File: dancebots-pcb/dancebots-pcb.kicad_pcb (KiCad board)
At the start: 2 copper layers, 50 x 50 mm, 33 parts, among them J1 BATTERY, J2 MOT2-L, J3 MOT1-R, J4 MP3 Player, U1 L4941, U2 L293, U3 ATTINY861A-P, U4 LM386, U5 LM358

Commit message: fixed silkscreen text to 2018 and 7.1
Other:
- board text added: "MP3 DanceBot V7.1 MINT&Pepper 2018"
- board text removed: "MP3 DanceBot V7 MINT&Pepper 2017"
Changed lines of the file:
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@@
   (page A4)
   (layers
-    (0 F.Cu signal)
-    (31 B.Cu signal)
+    (0 F.Cu signal hide)
+    (31 B.Cu signal hide)
     (32 B.Adhes user hide)
     (33 F.Adhes user hide)
     (34 B.Paste user hide)
     (35 F.Paste user hide)
-    (36 B.SilkS user)
+    (36 B.SilkS user hide)
     (37 F.SilkS user)
-    (38 B.Mask user)
-    (39 F.Mask user)
+    (38 B.Mask user hide)
+    (39 F.Mask user hide)
     (40 Dwgs.User user)
     (41 Cmts.User user)
@@
       (drillshape 0)
       (scaleselection 1)
-      (outputdirectory gerberv7.03/))
+      (outputdirectory gerberv7.1/))
   )
   (net 0 "")
@@
     (effects (font (size 1.2 1.2) (thickness 0.17)))
   )
-  (gr_text "MP3 DanceBot V7\nMINT&Pepper 2017" (at 147.75 101.95 90) (layer B.SilkS)
+  (gr_text "MP3 DanceBot V7.1\nMINT&Pepper 2018" (at 147.75 101.95 90) (layer B.SilkS)
     (effects (font (size 1.1 1.1) (thickness 0.17)) (justify left mirror))
   )

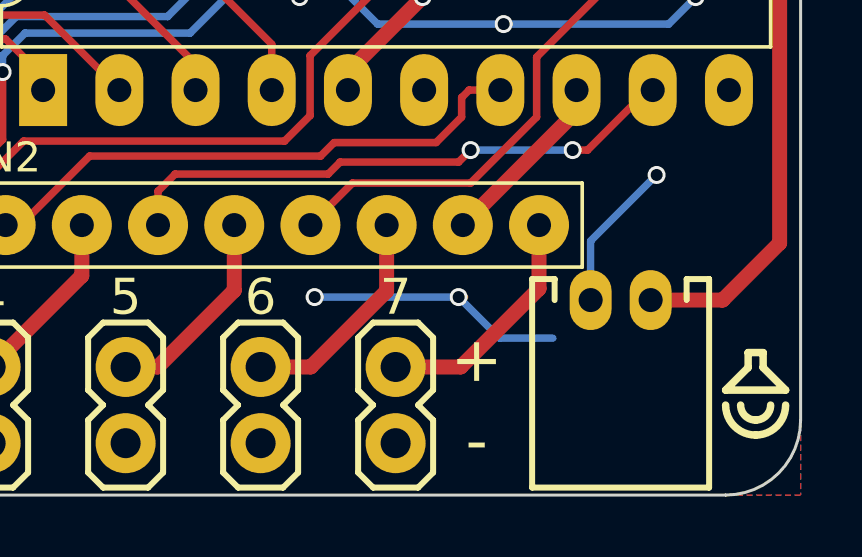
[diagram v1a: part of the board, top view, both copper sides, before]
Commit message: fixed broken ground plane connector near SPKR
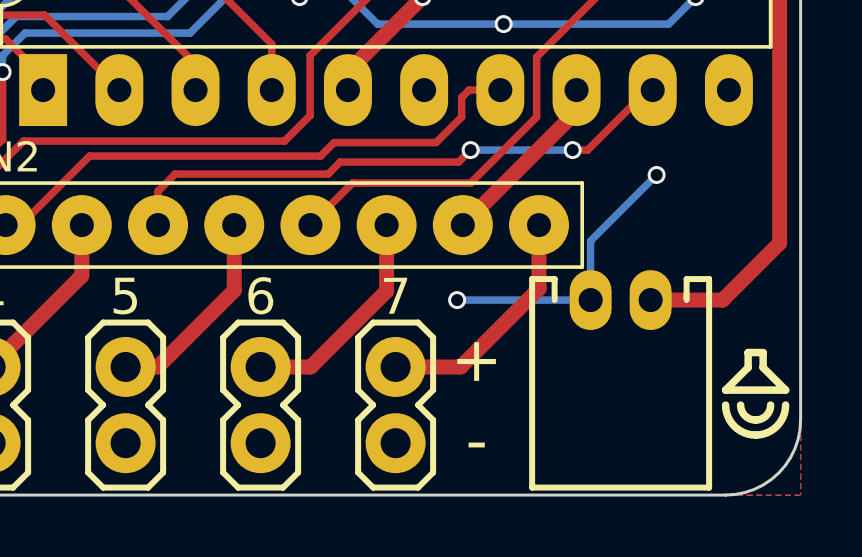
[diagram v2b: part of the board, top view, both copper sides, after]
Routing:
- net (no net): track 8.85 -> 0.00 mm, vias 2 -> 0
- net GND: track 173.4 -> 177.9 mm, vias 28 -> 29
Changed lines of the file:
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@@
     (thickness 1.6)
     (drawings 61)
-    (tracks 511)
+    (tracks 506)
     (zones 0)
     (modules 33)
@@
   (page A4)
   (layers
-    (0 F.Cu signal hide)
-    (31 B.Cu signal hide)
+    (0 F.Cu signal)
+    (31 B.Cu signal)
     (32 B.Adhes user hide)
     (33 F.Adhes user hide)
@@
   (gr_arc (start 102.5 102.5) (end 100 102.5) (angle 90) (layer Edge.Cuts) (width 0.1))
   (gr_line (start 102.5 100) (end 147.5 100) (angle 90) (layer Edge.Cuts) (width 0.1))
-  (segment (start 139.97 144.77) (end 138.6 143.4) (width 0.25) (layer B.Cu) (net 0))
-  (segment (start 141.74 144.77) (end 139.97 144.77) (width 0.25) (layer B.Cu) (net 0))
-  (segment (start 138.6 143.4) (end 133.8 143.4) (width 0.25) (layer B.Cu) (net 0))
-  (via (at 133.8 143.4) (size 0.6) (drill 0.4) (layers F.Cu B.Cu) (net 0))
-  (segment (start 138.6 143.4) (end 138.8 143.4) (width 0.25) (layer F.Cu) (net 0))
-  (via (at 138.6 143.4) (size 0.6) (drill 0.4) (layers F.Cu B.Cu) (net 0))
-  (segment (start 138.7 143.5) (end 138.6 143.4) (width 0.25) (layer B.Cu) (net 0))
   (segment (start 103.33 102.2) (end 103.33 105.87) (width 0.5) (layer F.Cu) (net 1))
   (segment (start 103.33 105.87) (end 103.3 105.9) (width 0.5) (layer F.Cu) (net 1))
@@
   (segment (start 103.4 119.7) (end 100.9 122.2) (width 0.5) (layer F.Cu) (net 1))
   (segment (start 103.4 117.44) (end 103.4 119.7) (width 0.5) (layer F.Cu) (net 1))
+  (segment (start 143 143.5) (end 138.55 143.5) (width 0.25) (layer B.Cu) (net 2) (status 400000))
+  (via (at 138.55 143.5) (size 0.6) (drill 0.4) (layers F.Cu B.Cu) (net 2))
   (segment (start 109.75 103.5) (end 108.3 103.5) (width 0.25) (layer F.Cu) (net 2))
   (segment (start 106.9 103.3) (end 107.65 104.05) (width 0.5) (layer B.Cu) (net 2))

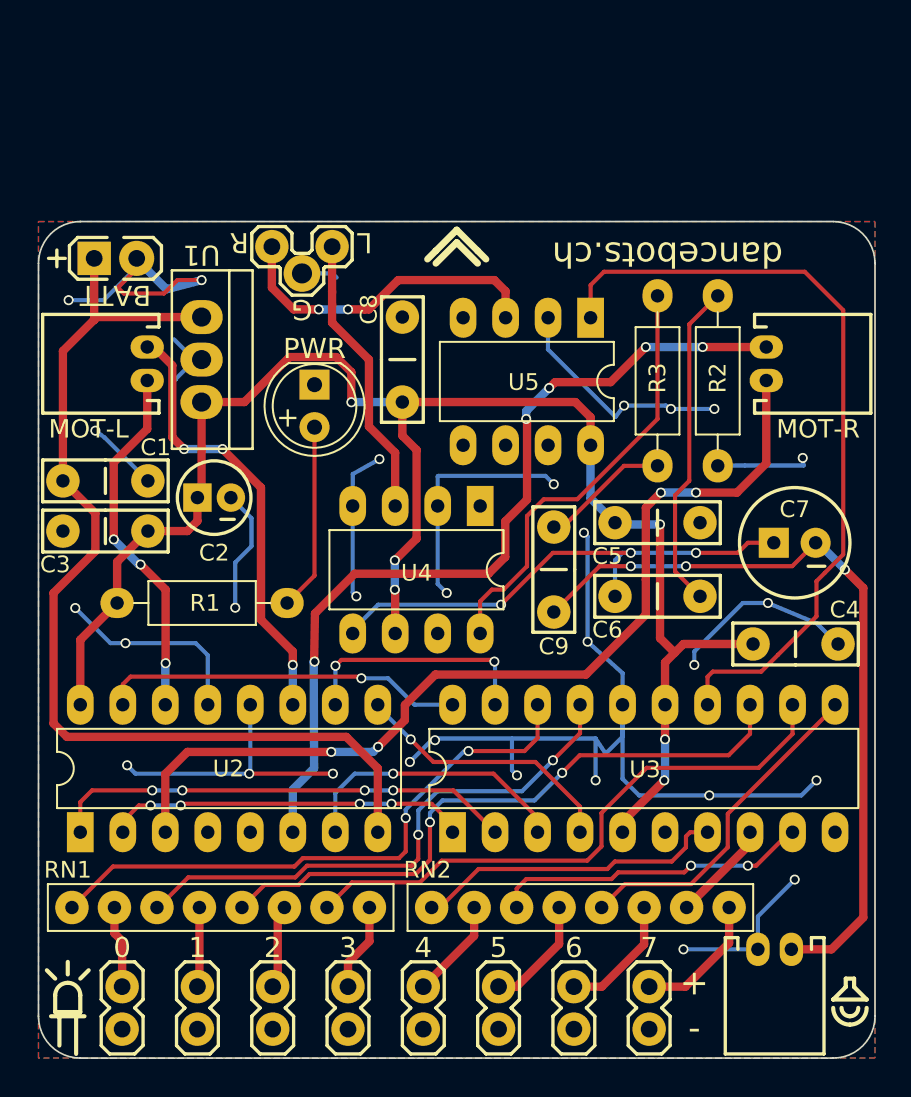
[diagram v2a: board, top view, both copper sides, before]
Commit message: v7.2: fixed symbol and library references, added part numbers, and cleaned up gnd vias on PCB
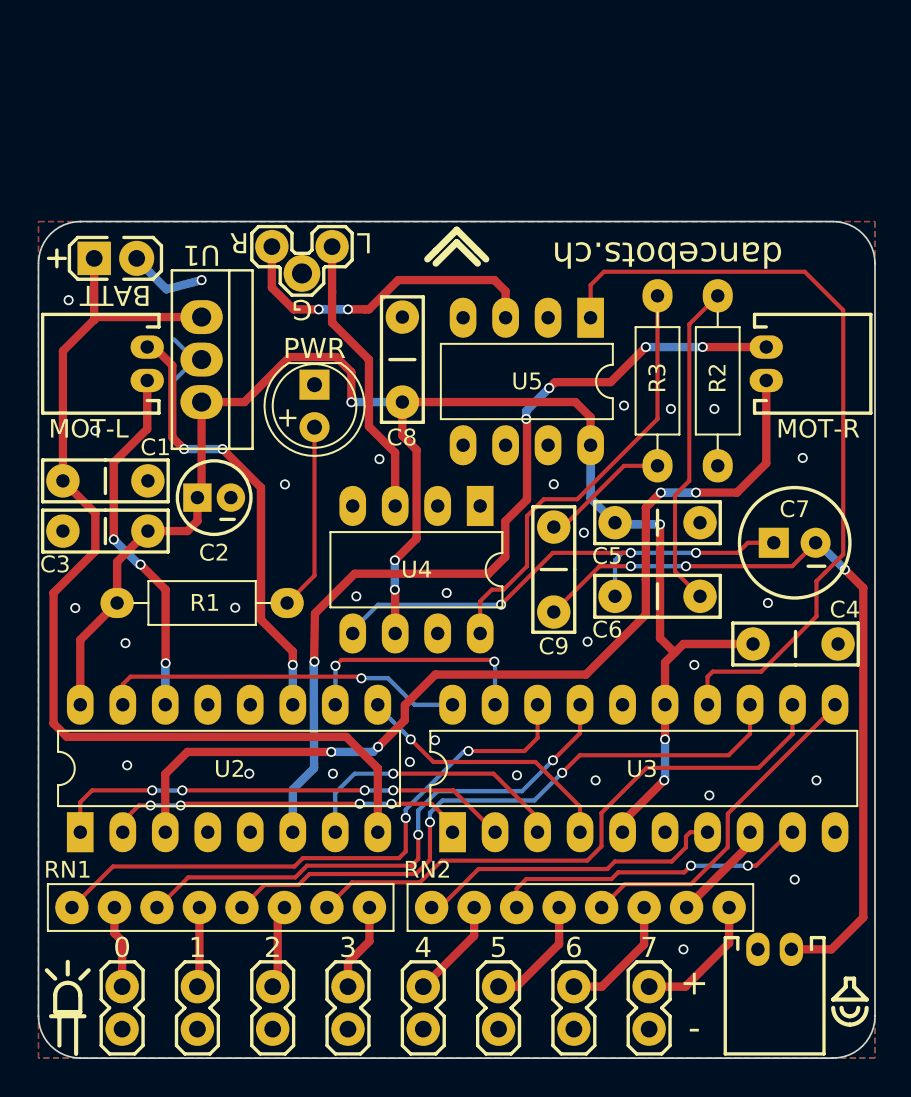
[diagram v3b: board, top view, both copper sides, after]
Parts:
- D0: footprint LEDs:LED_D5.0mm -> LED_THT:LED_D5.0mm
- U2: footprint Housings_DIP:DIP-16_W7.62mm_LongPads -> Package_DIP:DIP-16_W7.62mm_LongPads
- U3: value ATTINY861A-P -> ATTINY261A-P; footprint Housings_DIP:DIP-20_W7.62mm_LongPads -> Package_DIP:DIP-20_W7.62mm_LongPads
- U4, U5: footprint Housings_DIP:DIP-8_W7.62mm_LongPads -> Package_DIP:DIP-8_W7.62mm_LongPads
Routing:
- net GND: track 177.9 -> 10.9 mm, vias 29 -> 30
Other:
- board text added: "MP3 DanceBot V7.2 mint & pepper 2019"
- board text removed: "MP3 DanceBot V7.1 MINT&Pepper 2018"

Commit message: updated readme and added CERN license (also to PCB silkscreen)
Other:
- board text added: "Licensed under CERN OHL v.1.2"
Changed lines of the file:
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@@
   (general
     (thickness 1.6)
-    (drawings 61)
+    (drawings 62)
     (tracks 433)
     (zones 0)
@@
       (net 6 "Net-(C7-Pad2)"))
   )
+  (gr_text "Licensed under CERN OHL v.1.2" (at 132.512 100.978 180) (layer B.SilkS)
+    (effects (font (size 1.1 1.1) (thickness 0.17)) (justify mirror))
+  )
   (gr_line (start 123.75 101.75) (end 123.25 102.25) (angle 90) (layer F.SilkS) (width 0.4))
   (gr_line (start 126.25 101.75) (end 126.75 102.25) (angle 90) (layer F.SilkS) (width 0.4))
@@
     (effects (font (size 1.5 1.5) (thickness 0.2)))
   )
-  (gr_text "Designed in Switzerland" (at 135.1 102.05 180) (layer B.SilkS)
+  (gr_text "Designed in Switzerland" (at 129.21 102.756 180) (layer B.SilkS)
     (effects (font (size 1.1 1.1) (thickness 0.17)) (justify mirror))
   )
@@
   (gr_arc (start 102.5 102.5) (end 100 102.5) (angle 90) (layer Edge.Cuts) (width 0.1))
   (gr_line (start 102.5 100) (end 147.5 100) (angle 90) (layer Edge.Cuts) (width 0.1))
-  (via (at 114.732 115.71) (size 0.6) (drill 0.4) (layers F.Cu B.Cu) (net 2))
   (segment (start 103.33 102.2) (end 103.33 105.87) (width 0.5) (layer F.Cu) (net 1))
   (segment (start 103.33 105.87) (end 103.3 105.9) (width 0.5) (layer F.Cu) (net 1))
@@
   (segment (start 103.4 119.7) (end 100.9 122.2) (width 0.5) (layer F.Cu) (net 1))
   (segment (start 103.4 117.44) (end 103.4 119.7) (width 0.5) (layer F.Cu) (net 1))
+  (via (at 114.732 115.71) (size 0.6) (drill 0.4) (layers F.Cu B.Cu) (net 2))
   (via (at 138.55 143.5) (size 0.6) (drill 0.4) (layers F.Cu B.Cu) (net 2))
   (segment (start 106.9 103.3) (end 107.65 104.05) (width 0.5) (layer B.Cu) (net 2))

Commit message: migrated to Kicad 6.0
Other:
- net class Default removed

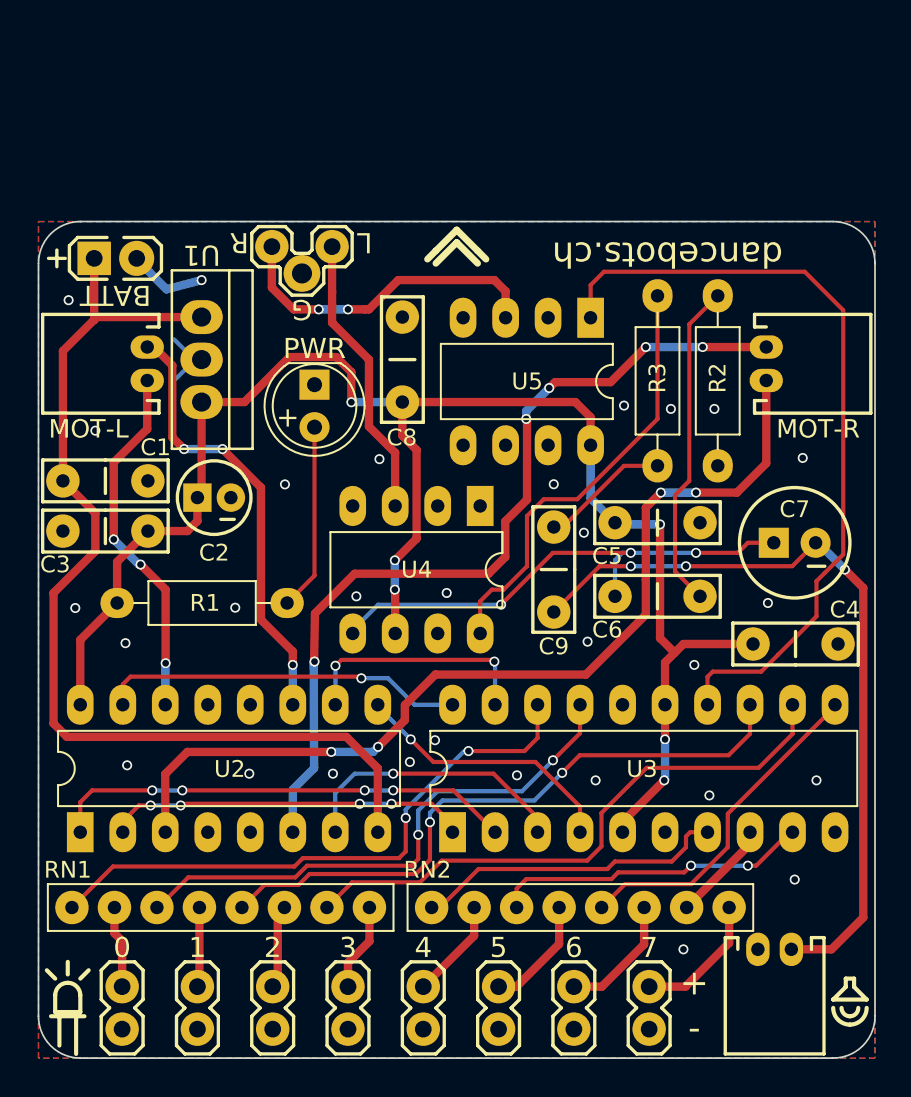
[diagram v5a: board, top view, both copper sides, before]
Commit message: V8.0, MP3 Player integrated
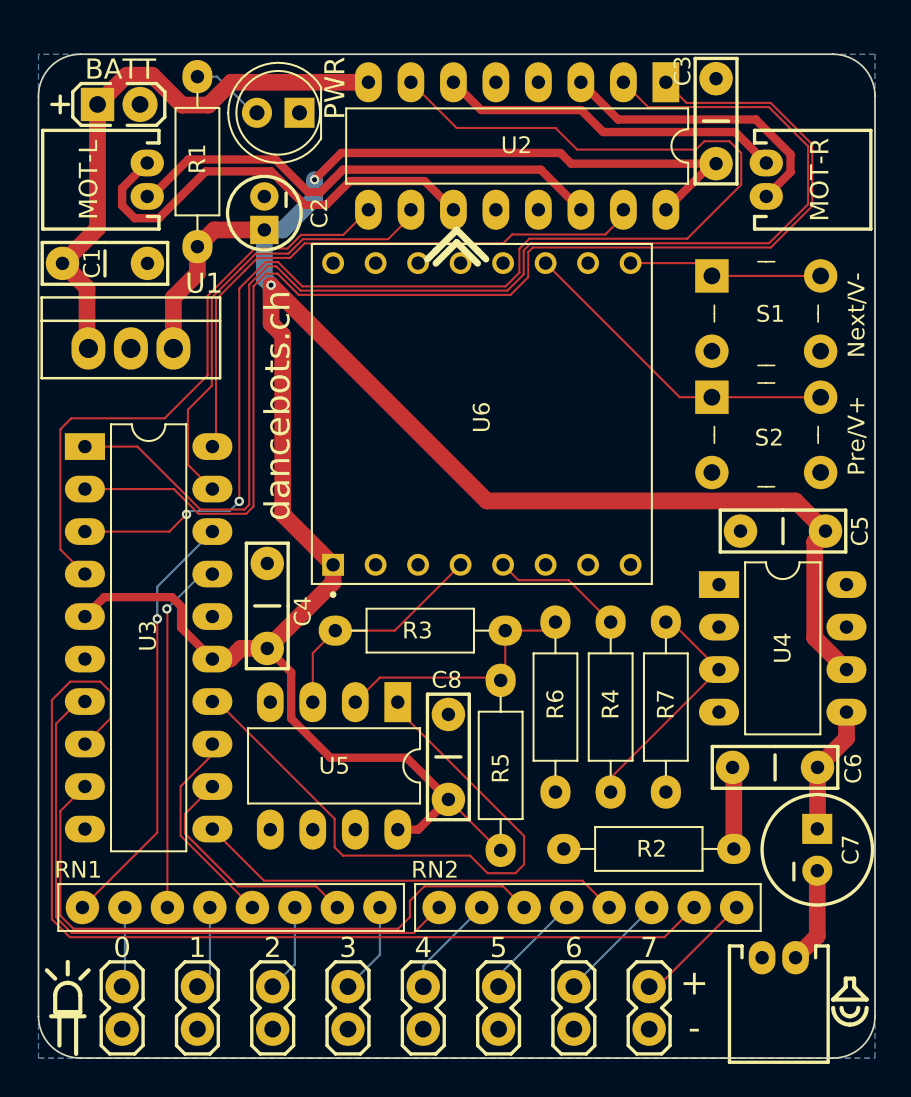
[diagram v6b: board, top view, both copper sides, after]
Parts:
- removed C9: 10pF, dancebots_fp:CAPC
- removed J4: MP3 Player, dancebots_fp:MP3
- added R4: 10k, dancebots_fp:RES, F.Cu at (134.2, 134.1)
- added R5: 10k, dancebots_fp:RES, F.Cu at (127.6, 127.4)
- added R6: 10k, dancebots_fp:RES, F.Cu at (130.9, 134.1)
- added R7: 10k, dancebots_fp:RES, F.Cu at (137.5, 134.1)
- added S1: MJTP1230, digikey-footprints:Switch_Tactile_THT_6x6mm_MJTP1230, F.Cu at (140.2, 103.2)
- added S2: MJTP1230, digikey-footprints:Switch_Tactile_THT_6x6mm_MJTP1230, F.Cu at (140.2, 110.5)
- added U6: DFR0299, dancebots_fp:MODULE_DFR0299, F.Cu at (126.5, 111.5)
- R3: value 10 -> 10k
- moved U2 56.9 mm to (137.5, 91.7), turned to -90 degrees
- moved C3 44.0 mm to (140.5, 94.0), turned to 90 degrees
- moved U3 31.8 mm to (102.8, 113.5), turned to 0 degrees
- moved C4 31.7 mm to (113.7, 123.0), turned to 90 degrees
- moved U5 25.7 mm to (121.5, 128.7)
- moved R2 24.7 mm to (131.4, 137.5), turned to 0 degrees
- moved C8 23.9 mm to (124.5, 132.0)
- moved R1 21.8 mm to (109.5, 101.5), turned to 90 degrees
- moved C7 18.4 mm to (146.6, 137.6), turned to -90 degrees
- moved C2 17.3 mm to (113.5, 99.5), turned to 90 degrees
- moved D0 16.3 mm to (115.6, 93.5), turned to 180 degrees
- moved U4 15.0 mm to (140.7, 121.7), turned to 0 degrees
- moved R3 13.4 mm to (127.9, 124.5), turned to 180 degrees
- moved C1 13.0 mm to (104.0, 102.5)
- moved C6 12.4 mm to (144.0, 132.6), turned to 180 degrees
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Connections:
- net Net-(C6-Pad1) renamed /ph_md
- net Net-(C6-Pad2) renamed /ph_dc
- net Net-(C7-Pad2) renamed /ph_ac
- R3 pad 1: Net-(C9-Pad1) -> Net-(R3-Pad1)
- R3 pad 2: Net-(R3-Pad2) -> /MP3_R
- U3 pad 10: Net-(U3-Pad10) -> unconnected-(U3-Pad10)
- U4 pad 1: Net-(U4-Pad1) -> unconnected-(U4-Pad1)
- U4 pad 3: /MP3_L -> Net-(R4-Pad1)
- U4 pad 8: Net-(R3-Pad2) -> unconnected-(U4-Pad8)
- U5 pad 2: GND -> Net-(R3-Pad1)
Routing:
- net /D1B: track 16.9 -> 81.1 mm, vias 1 -> 2
- net +5V: track 98.8 -> 160.2 mm, vias 6 -> 2
- net /D1A: track 21.8 -> 78.2 mm, vias 4 -> 0
- net /LED7: track 6.07 -> 60.6 mm
- net /PWM1: track 28.6 -> 75.3 mm, vias 4 -> 0
- net /ph_ac: track 46.1 -> 5.74 mm, vias 3 -> 0
- net /MOT1+: track 56.3 -> 17.4 mm, vias 4 -> 0
- net /MOT1-: track 51.6 -> 20.7 mm, vias 5 -> 0
- net +BATT: track 61.3 -> 34.3 mm
- net Net-(R3-Pad2): track 26.2 -> 0.00 mm
- net /LED2: track 38.0 -> 12.3 mm, vias 2 -> 0
- net /ph_dc: track 30.8 -> 7.70 mm, vias 3 -> 0
- net /LED3: track 35.0 -> 14.4 mm
- net Net-(S2-Pad1): track 0.00 -> 19.8 mm
- net /PWM2: track 16.2 -> 35.9 mm, vias 1 -> 0
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- removed copper zone on F.Cu, net GND
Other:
- board size 50 x 50 mm -> 50 x 60 mm
- board text added: "MP3 DanceBot V8.0 mint & pepper 2022"
- board text added: "Next/V-"
- board text added: "Pre/V+"
- board text removed: "G"
- board text removed: "L"
- board text removed: "MP3 DanceBot V7.2 mint & pepper 2019"
- board text removed: "R"

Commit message: V8.1: Changed DFplayer Mini to oblong holes for beveled headers
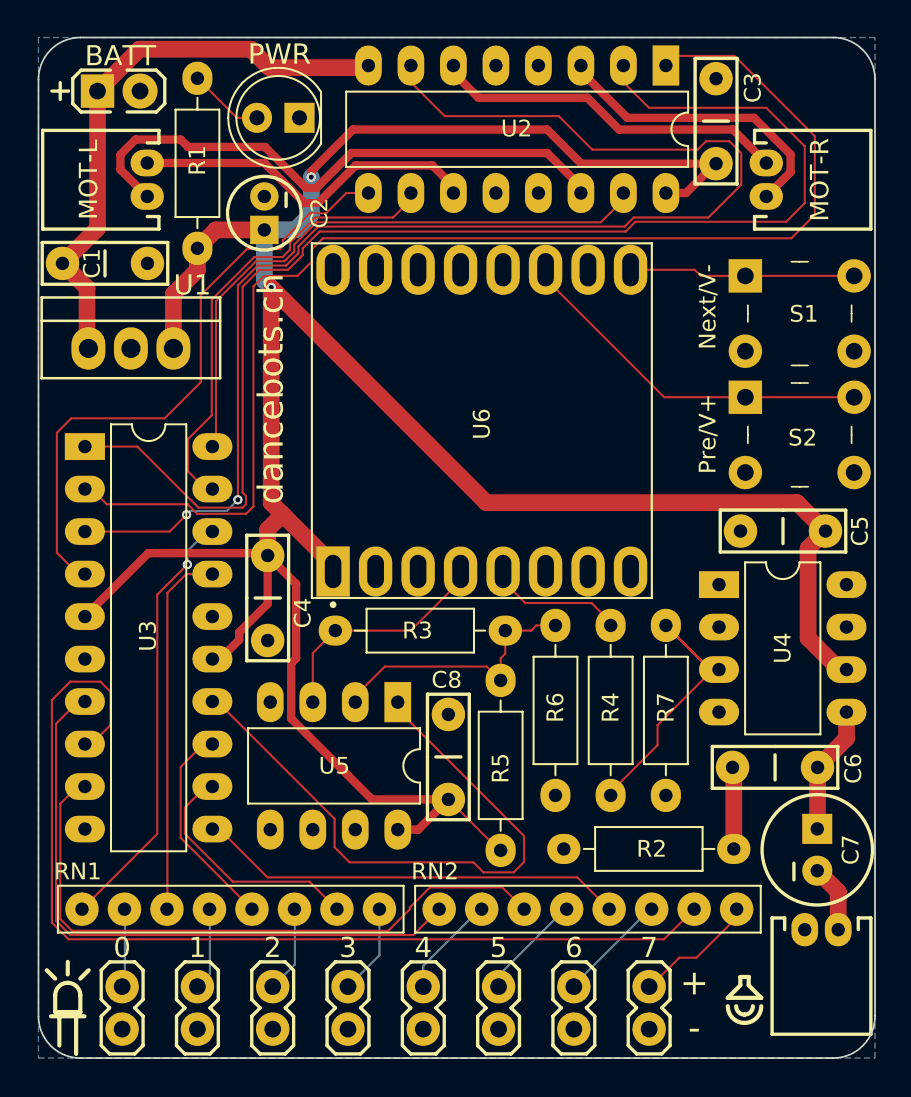
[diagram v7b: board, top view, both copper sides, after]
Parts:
- moved JP18 3.05 mm to (146.8, 142.3)
- moved S1 2.00 mm to (142.2, 103.2)
- moved S2 2.00 mm to (142.2, 110.5)
- moved U2 1.00 mm to (137.5, 90.7)
- moved J1 0.80 mm to (104.8, 92.2)
- moved C4 0.48 mm to (113.7, 122.5), turned to -90 degrees
- moved U6 0.40 mm to (126.5, 111.9)
- moved D0 0.30 mm to (115.6, 93.8)
- moved R4 0.20 mm to (134.2, 134.3)
- moved R6 0.20 mm to (130.9, 134.3)
- moved R7 0.20 mm to (137.5, 134.3)
- moved RN1 0.10 mm to (102.6, 141.1)
- moved R1 0.10 mm to (109.5, 101.6)
- moved RN2 0.10 mm to (124.0, 141.1)
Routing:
- net +5V: track 160.2 -> 169.1 mm
- net /MOT2-: track 26.6 -> 20.7 mm
- net /MOT2+: track 29.2 -> 34.0 mm
- net Net-(R4-Pad1): track 14.4 -> 17.9 mm
- net /D1A: track 78.2 -> 76.0 mm
- net Net-(S1-Pad1): track 11.7 -> 13.5 mm
- net /D1B: track 81.1 -> 79.4 mm
- net /ph_ac: track 5.74 -> 4.04 mm
- net Net-(S2-Pad1): track 19.8 -> 21.4 mm
- net Net-(LED5-Pad2): track 6.42 -> 4.91 mm
- net /LED1: track 21.4 -> 22.5 mm, vias 1 -> 0
- net /PWM1: track 75.3 -> 74.4 mm
- net Net-(LED6-Pad2): track 6.66 -> 5.73 mm
- net /PWM2: track 35.9 -> 36.8 mm
- net /DATA: track 36.9 -> 36.0 mm
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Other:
- board size 50 x 60 mm -> 50 x 61 mm
- board text added: "MP3 DanceBot V8.1 mint & pepper 2022"
- board text removed: "MP3 DanceBot V8.0 mint & pepper 2022"
